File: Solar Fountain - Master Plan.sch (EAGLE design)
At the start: 0 parts

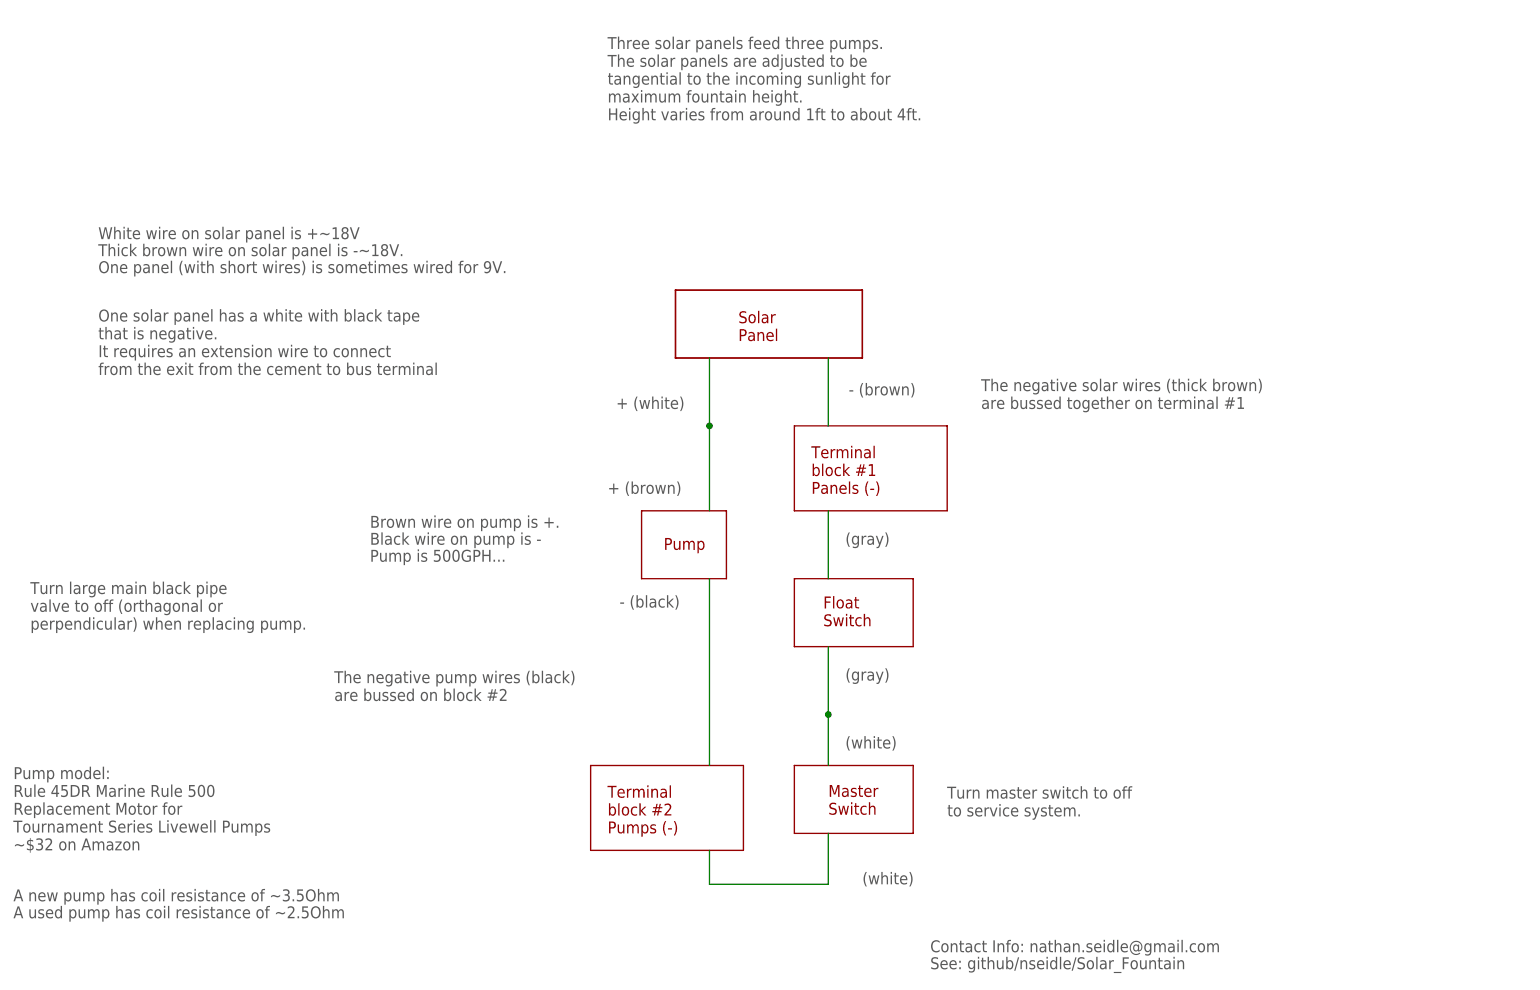
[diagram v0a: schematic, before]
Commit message: Added notes about panel labels and how to test panel and pumps for problems.
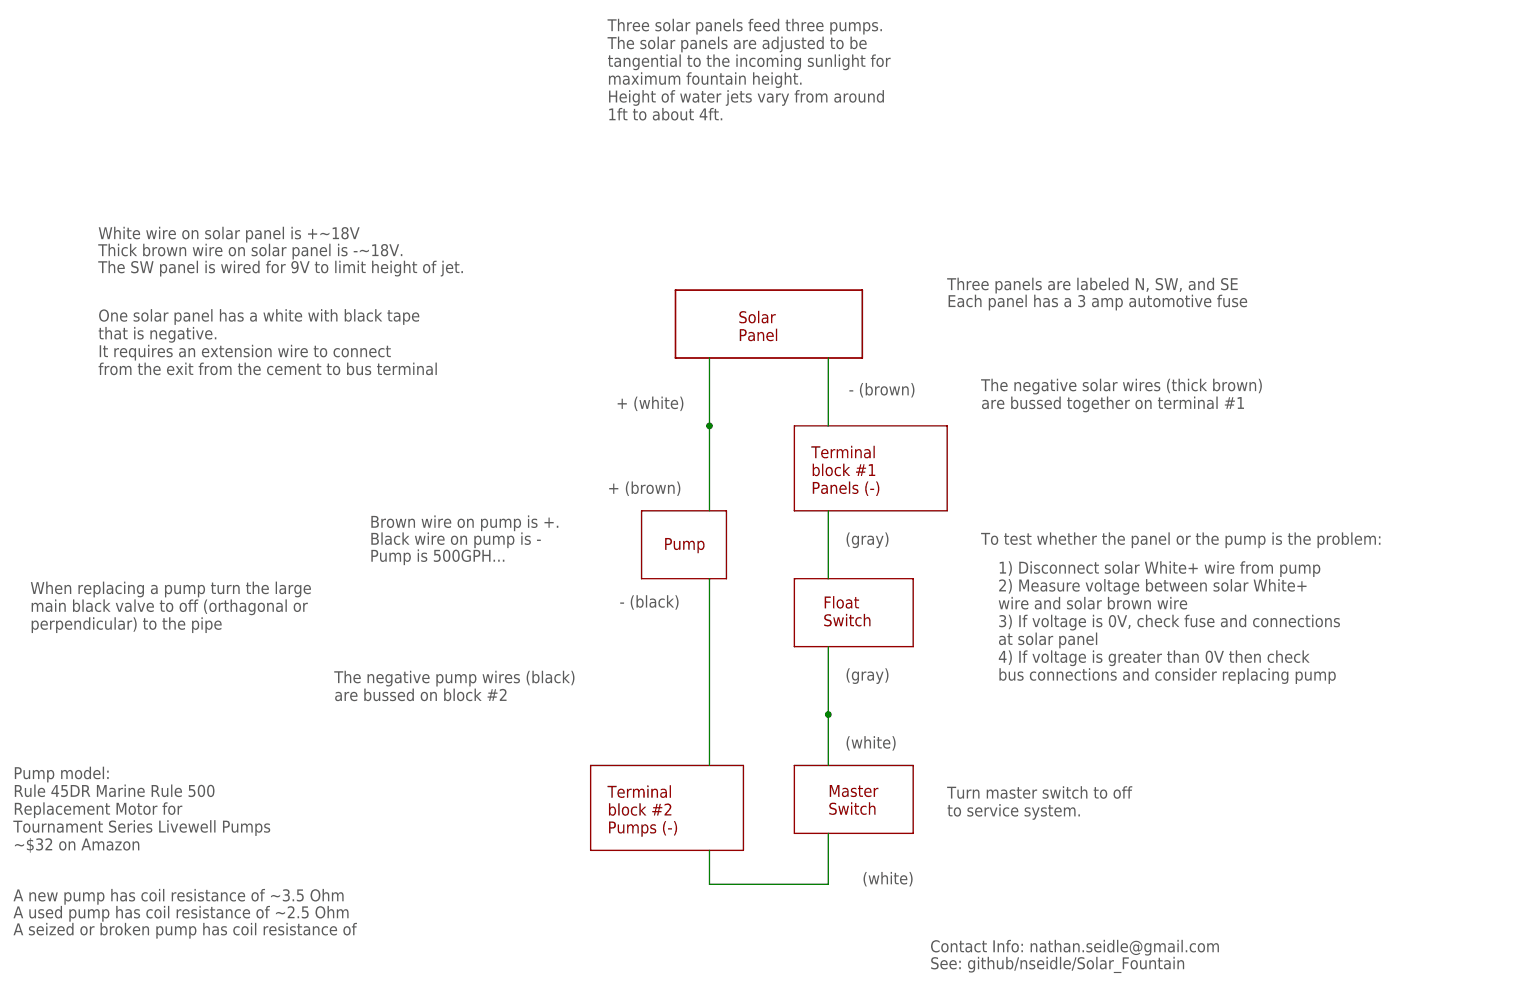
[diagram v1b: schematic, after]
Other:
- note added: "1) Disconnect solar White+ wire from pump 2) Measure voltage between solar White+ wire and solar brown wire 3) If voltage is 0V, check fuse and connections at solar panel 4) If voltage is greater than 0V then check bus connections and consider replacing pump"
- note added: "A new pump has coil resistance of ~3.5 Ohm"
- note added: "A seized or broken pump has coil resistance of"
- note added: "A used pump has coil resistance of ~2.5 Ohm"
- note added: "Each panel has a 3 amp automotive fuse"
- note added: "The SW panel is wired for 9V to limit height of jet."
- note added: "Three panels are labeled N, SW, and SE"
- note added: "Three solar panels feed three pumps. The solar panels are adjusted to be tangential to the incoming sunlight for maximum fountain height. Height of water jets vary from around 1ft to about 4ft."
- note added: "To test whether the panel or the pump is the problem:"
- note added: "When replacing a pump turn the large main black valve to off (orthagonal or perpendicular) to the pipe"
- note removed: "A new pump has coil resistance of ~3.5Ohm"
- note removed: "A used pump has coil resistance of ~2.5Ohm"
- note removed: "One panel (with short wires) is sometimes wired for 9V."
- note removed: "Three solar panels feed three pumps. The solar panels are adjusted to be tangential to the incoming sunlight for maximum fountain height. Height varies from around 1ft to about 4ft."
- note removed: "Turn large main black pipe valve to off (orthagonal or perpendicular) when replacing pump."
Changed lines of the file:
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@@
 <?xml version="1.0" encoding="utf-8"?>
 <!DOCTYPE eagle SYSTEM "eagle.dtd">
-<eagle version="6.5.0">
+<eagle version="7.2.0">
 <drawing>
 <settings>
@@
 <layer number="254" name="cooling" color="7" fill="1" visible="yes" active="yes"/>
 </layers>
-<schematic>
+<schematic xreflabel="%F%N/%S" xrefpart="/%S.%C%R">
 <attributes>
 </attributes>
@@
 <text x="22.86" y="149.86" size="1.778" layer="97">White wire on solar panel is +~18V</text>
 <text x="22.86" y="147.32" size="1.778" layer="97">Thick brown wire on solar panel is -~18V.</text>
-<text x="22.86" y="144.78" size="1.778" layer="97">One panel (with short wires) is sometimes wired for 9V.</text>
+<text x="22.86" y="144.78" size="1.778" layer="97">The SW panel is wired for 9V to limit height of jet.</text>
 <text x="63.5" y="101.6" size="1.778" layer="97">Pump is 500GPH...</text>
 <text x="154.94" y="124.46" size="1.778" layer="97">The negative solar wires (thick brown)
@@
 It requires an extension wire to connect
 from the exit from the cement to bus terminal</text>
-<text x="12.7" y="91.44" size="1.778" layer="97">Turn large main black pipe
-valve to off (orthagonal or
-perpendicular) when replacing pump.</text>
+<text x="12.7" y="91.44" size="1.778" layer="97">When replacing a pump turn the large
+main black valve to off (orthagonal or
+perpendicular) to the pipe</text>
 <text x="129.54" y="111.76" size="1.778" layer="94">Terminal
 block #1
@@
 <text x="134.62" y="83.82" size="1.778" layer="97">(gray)</text>
 <text x="134.62" y="104.14" size="1.778" layer="97">(gray)</text>
-<text x="10.16" y="50.8" size="1.778" layer="97">A new pump has coil resistance of ~3.5Ohm</text>
-<text x="10.16" y="48.26" size="1.778" layer="97">A used pump has coil resistance of ~2.5Ohm</text>
+<text x="10.16" y="50.8" size="1.778" layer="97">A new pump has coil resistance of ~3.5 Ohm</text>
+<text x="10.16" y="48.26" size="1.778" layer="97">A used pump has coil resistance of ~2.5 Ohm</text>
 <text x="99.06" y="167.64" size="1.778" layer="97">Three solar panels feed three pumps.
 The solar panels are adjusted to be
 tangential to the incoming sunlight for
 maximum fountain height.
-Height varies from around 1ft to about 4ft.</text>
+Height of water jets vary from around
+1ft to about 4ft.</text>
+<text x="149.86" y="142.24" size="1.778" layer="97">Three panels are labeled N, SW, and SE</text>
+<text x="10.16" y="45.72" size="1.778" layer="97">A seized or broken pump has coil resistance of</text>
+<text x="149.86" y="139.7" size="1.778" layer="97">Each panel has a 3 amp automotive fuse</text>
+<text x="154.94" y="104.14" size="1.778" layer="97">To test whether the panel or the pump is the problem:</text>
+<text x="157.48" y="83.82" size="1.778" layer="97">1) Disconnect solar White+ wire from pump
+2) Measure voltage between solar White+
+wire and solar brown wire
+3) If voltage is 0V, check fuse and connections
+at solar panel
+4) If voltage is greater than 0V then check
+bus connections and consider replacing pump</text>
 </plain>
 <instances>
